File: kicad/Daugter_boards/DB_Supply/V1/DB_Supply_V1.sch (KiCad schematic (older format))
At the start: 30 parts, among them U1 LM555N

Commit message: update MDL and DB Supply
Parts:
- removed +12V1, +5V1: LM2940, symbol 78L05
- removed +3.3V: LM1117T, symbol 78L05
- removed -12V1, -5V1: LM2990, symbol 78L05
- added U2: LM2940T-12.0/NOPB, symbol LM2940T-12.0/NOPB
- added U3: LM2940T-5.0/NOPB, symbol LM2940T-5.0/NOPB
- added U4: LM1117T-3.3/NOPB, symbol LM1117T-3.3/NOPB
- added U5: LM2990T-12.0/NOPB, symbol LM2990T-12.0/NOPB
- added U6: LM2990T-5.0/NOPB, symbol LM2990T-5.0/NOPB
- D1: renamed from 1N400X1; value D -> 1N4001
- D2: renamed from 1N400X2; value D -> 1N4001
- D3: renamed from 1N400X3; value D -> 1N4001
- Q1: renamed from 2N2222; value Q_NPN_BCE -> Q2N2222
- Q2: renamed from 2N2222_1; value Q_NPN_BCE -> Q2N2222
- Q3: renamed from 2N2907; value Q_PNP_BCE -> Q2N2907
- gave numbers to parts that had none: 3
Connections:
- net at C9.1, P1.2 (P2), P2.2 (P2)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: now also U3.VO
- net at C1.1, C10.2, C2.1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: now also U2.GND, U3.GND, U4.GND, U5.GND, U6.GND
- net at C8.1, P1.6 (P6), P2.6 (P6): now also U2.VO, U3.VI, U4.VI
- net at C4.2, D3.2 (A): now also U5.VI
- net at C5.2, P1.8 (P8), P2.8 (P8): now also U5.VO, U6.VI
- net at C6.2, P1.18 (P18), P2.18 (P18): now also U6.VO
- net at C10.1, P1.19 (P19), P2.19 (P19): now also U4.VO
- net 18V: no longer names the net of C7.1, D1.1 (K), Q2.2 (C), R4.1
- net 18V: now also U2.VI
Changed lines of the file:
@@
 LIBS:contrib
 LIBS:valves
+LIBS:echopen
+LIBS:DB_Supply_V1-cache
 EELAYER 25 0
 EELAYER END
@@
 NoConn ~ 4750 3700
 $Comp
-L D 1N400X1
+L D D1
 U 1 1 572A15CB
 P 4900 5350
-F 0 "1N400X1" H 4900 5450 50  0000 C CNN
-F 1 "D" H 4900 5250 50  0000 C CNN
+F 0 "D1" H 4900 5450 50  0000 C CNN
+F 1 "1N4001" H 4900 5250 50  0000 C CNN
 F 2 "" H 4900 5350 50  0000 C CNN
 F 3 "" H 4900 5350 50  0000 C CNN
@@
 Connection ~ 6950 5800
 $Comp
-L Q_NPN_BCE 2N2222
+L Q_NPN_BCE Q1
 U 1 1 572A387C
 P 5600 3700
-F 0 "2N2222" H 5900 3750 50  0000 R CNN
-F 1 "Q_NPN_BCE" H 6200 3650 50  0000 R CNN
+F 0 "Q1" H 5900 3750 50  0000 R CNN
+F 1 "Q2N2222" H 6200 3650 50  0000 R CNN
 F 2 "" H 5800 3800 50  0000 C CNN
 F 3 "" H 5600 3700 50  0000 C CNN
@@
 	5050 3200 6600 3200
 $Comp
-L Q_NPN_BCE 2N2222_1
+L Q_NPN_BCE Q2
 U 1 1 572A3ACF
 P 6500 3400
-F 0 "2N2222_1" H 6800 3450 50  0000 R CNN
-F 1 "Q_NPN_BCE" H 7100 3350 50  0000 R CNN
+F 0 "Q2" H 6800 3450 50  0000 R CNN
+F 1 "Q2N2222" H 7100 3350 50  0000 R CNN
 F 2 "" H 6700 3500 50  0000 C CNN
 F 3 "" H 6500 3400 50  0000 C CNN
@@
 $EndComp
 $Comp
-L Q_PNP_BCE 2N2907
+L Q_PNP_BCE Q3
 U 1 1 572A3B5B
 P 6500 3800
-F 0 "2N2907" H 6800 3850 50  0000 R CNN
-F 1 "Q_PNP_BCE" H 7100 3750 50  0000 R CNN
+F 0 "Q3" H 6800 3850 50  0000 R CNN
+F 1 "Q2N2907" H 7100 3750 50  0000 R CNN
 F 2 "" H 6700 3900 50  0000 C CNN
 F 3 "" H 6500 3800 50  0000 C CNN
@@
 $EndComp
 $Comp
-L D 1N400X2
+L D D2
 U 1 1 572A3EDF
 P 7500 3750
-F 0 "1N400X2" H 7500 3850 50  0000 C CNN
-F 1 "D" H 7500 3650 50  0000 C CNN
+F 0 "D2" H 7500 3850 50  0000 C CNN
+F 1 "1N4001" H 7500 3650 50  0000 C CNN
 F 2 "" H 7500 3750 50  0000 C CNN
 F 3 "" H 7500 3750 50  0000 C CNN
@@
 $EndComp
 $Comp
-L D 1N400X3
+L D D3
 U 1 1 572A4183
 P 7650 3600
-F 0 "1N400X3" H 7650 3700 50  0000 C CNN
-F 1 "D" H 7650 3500 50  0000 C CNN
+F 0 "D3" H 7650 3700 50  0000 C CNN
+F 1 "1N4001" H 7650 3500 50  0000 C CNN
 F 2 "" H 7650 3600 50  0000 C CNN
 F 3 "" H 7650 3600 50  0000 C CNN
@@
 	5050 3200 5050 5500
 NoConn ~ 5050 3700
-$Comp
-L 78L05 -12V1
-U 1 1 575A0CF3
-P 8200 3650
-F 0 "-12V1" H 8350 3454 50  0000 C CNN
-F 1 "LM2990" H 8200 3850 50  0000 C CNN
-F 2 "" H 8200 3650 50  0000 C CNN
-F 3 "" H 8200 3650 50  0000 C CNN
-	1    8200 3650
-	1    0    0    -1
-$EndComp
-$Comp
-L 78L05 -5V1
-U 1 1 575A10F8
-P 9000 3650
-F 0 "-5V1" H 9150 3454 50  0000 C CNN
-F 1 "LM2990" H 9000 3850 50  0000 C CNN
-F 2 "" H 9000 3650 50  0000 C CNN
-F 3 "" H 9000 3650 50  0000 C CNN
-	1    9000 3650
-	1    0    0    -1
-$EndComp
 Connection ~ 8600 3600
 Wire Wire Line
@@
 	9400 4000 9400 3900
 Connection ~ 9000 4000
-$Comp
-L 78L05 +12V1
-U 1 1 575A672C
-P 5450 5400
-F 0 "+12V1" H 5600 5204 50  0000 C CNN
-F 1 "LM2940" H 5450 5600 50  0000 C CNN
-F 2 "" H 5450 5400 50  0000 C CNN
-F 3 "" H 5450 5400 50  0000 C CNN
-	1    5450 5400
-	1    0    0    -1
-$EndComp
-$Comp
-L 78L05 +5V1
-U 1 1 575A9393
-P 6250 5400
-F 0 "+5V1" H 6400 5204 50  0000 C CNN
-F 1 "LM2940" H 6250 5600 50  0000 C CNN
-F 2 "" H 6250 5400 50  0000 C CNN
-F 3 "" H 6250 5400 50  0000 C CNN
-	1    6250 5400
-	1    0    0    -1
-$EndComp
 Wire Wire Line
 	5850 4350 5850 5500
@@
 Connection ~ 7500 3600
 Connection ~ 5700 3500
-Text Label 6100 3200 0    60   ~ 0
-18V
 Text Label 8150 7650 0    60   ~ 0
 03/08/2016
@@
 Supply_daugter_board
 $Comp
-L CONN_01X19 P?
+L CONN_01X19 P1
 U 1 1 57A1CA2F
 P 2350 4850
-F 0 "P?" H 2350 5850 50  0000 C CNN
+F 0 "P1" H 2350 5850 50  0000 C CNN
 F 1 "CONN_01X19" V 2450 4850 50  0000 C CNN
 F 2 "" H 2350 4850 50  0000 C CNN
@@
 Wire Wire Line
 	8600 2850 8600 3600
-$Comp
-L 78L05 +3.3V
-U 1 1 57A2E6B8
-P 6300 4400
-F 0 "+3.3V" H 6450 4204 50  0000 C CNN
-F 1 "LM1117T" H 6300 4600 50  0000 C CNN
-F 2 "" H 6300 4400 50  0000 C CNN
-F 3 "" H 6300 4400 50  0000 C CNN
-	1    6300 4400
-	1    0    0    -1
-$EndComp
 Wire Wire Line
 	5850 4350 5900 4350
 Connection ~ 5850 5050
 $Comp
-L CP C?
+L CP C10
 U 1 1 57A2E7D0
 P 6700 4500
-F 0 "C?" H 6725 4600 50  0000 L CNN
+F 0 "C10" H 6725 4600 50  0000 L CNN
 F 1 "47u" H 6725 4400 50  0000 L CNN
 F 2 "" H 6738 4350 50  0000 C CNN
@@
 NoConn ~ 5850 4850
 $Comp
-L CONN_01X19 P?
+L CONN_01X19 P2
 U 1 1 57A31EE2
 P 10650 4850
-F 0 "P?" H 10650 5850 50  0000 C CNN
+F 0 "P2" H 10650 5850 50  0000 C CNN
 F 1 "CONN_01X19" V 10750 4850 50  0000 C CNN
 F 2 "" H 10650 4850 50  0000 C CNN
@@
 NoConn ~ 9900 3950
 NoConn ~ 9900 4050
+$Comp
+L LM2940T-12.0/NOPB U2
+U 1 1 57AB2B24
+P 5450 5400
+F 0 "U2" H 5600 5204 50  0000 C CNN
+F 1 "LM2940T-12.0/NOPB" H 5450 5600 50  0000 C CNN
+F 2 "" H 5450 5400 50  0000 C CNN
+F 3 "" H 5450 5400 50  0000 C CNN
+	1    5450 5400
+	1    0    0    -1
+$EndComp
+$Comp
+L LM2940T-5.0/NOPB U3
+U 1 1 57AB2BC1
+P 6250 5400
+F 0 "U3" H 6400 5204 50  0000 C CNN
+F 1 "LM2940T-5.0/NOPB" H 6250 5600 50  0000 C CNN
+F 2 "" H 6250 5400 50  0000 C CNN
+F 3 "" H 6250 5400 50  0000 C CNN
+	1    6250 5400
+	1    0    0    -1
+$EndComp
+$Comp
+L LM1117T-3.3/NOPB U4
+U 1 1 57AB2C54
+P 6300 4400
+F 0 "U4" H 6450 4204 50  0000 C CNN
+F 1 "LM1117T-3.3/NOPB" H 6300 4600 50  0000 C CNN
+F 2 "" H 6300 4400 50  0000 C CNN
+F 3 "" H 6300 4400 50  0000 C CNN
+	1    6300 4400
+	1    0    0    -1
+$EndComp
+$Comp
+L LM2990T-12.0/NOPB U5
+U 1 1 57AB4084
+P 8200 3650
+F 0 "U5" H 8350 3454 50  0000 C CNN
+F 1 "LM2990T-12.0/NOPB" H 8200 3850 50  0000 C CNN
+F 2 "" H 8200 3650 50  0000 C CNN
+F 3 "" H 8200 3650 50  0000 C CNN
+	1    8200 3650
+	1    0    0    -1
+$EndComp
+$Comp
+L LM2990T-5.0/NOPB U6
+U 1 1 57AB4135
+P 9000 3650
+F 0 "U6" H 9150 3454 50  0000 C CNN
+F 1 "LM2990T-5.0/NOPB" H 9000 3850 50  0000 C CNN
+F 2 "" H 9000 3650 50  0000 C CNN
+F 3 "" H 9000 3650 50  0000 C CNN
+	1    9000 3650
+	1    0    0    -1
+$EndComp
 $EndSCHEMATC

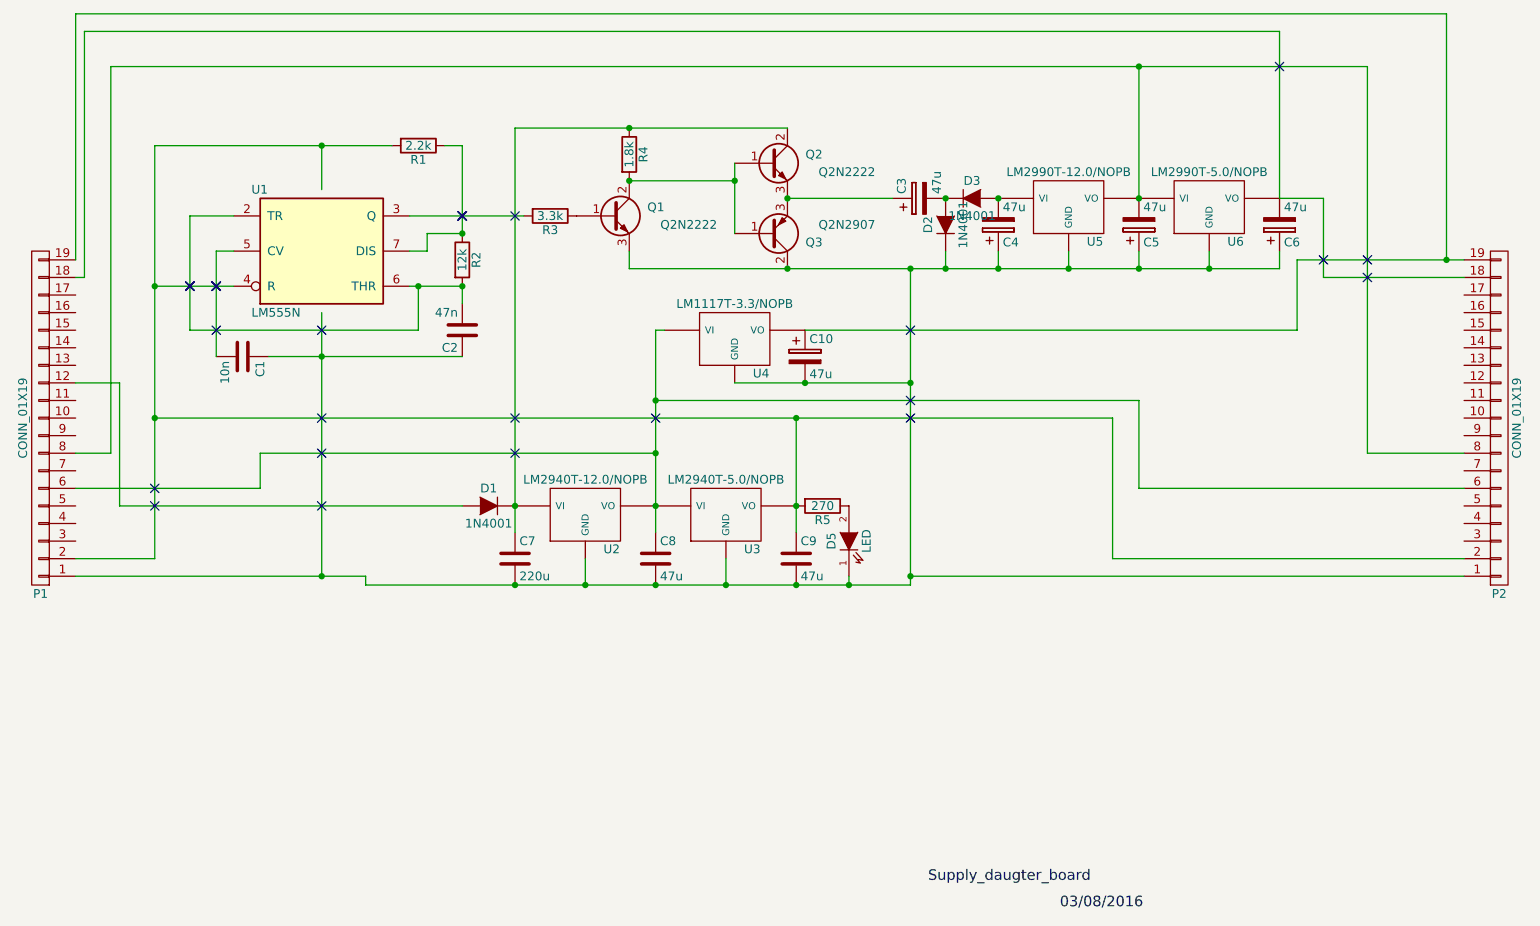
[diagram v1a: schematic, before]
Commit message: update DB_HV, update librairy and librairy path for MDL
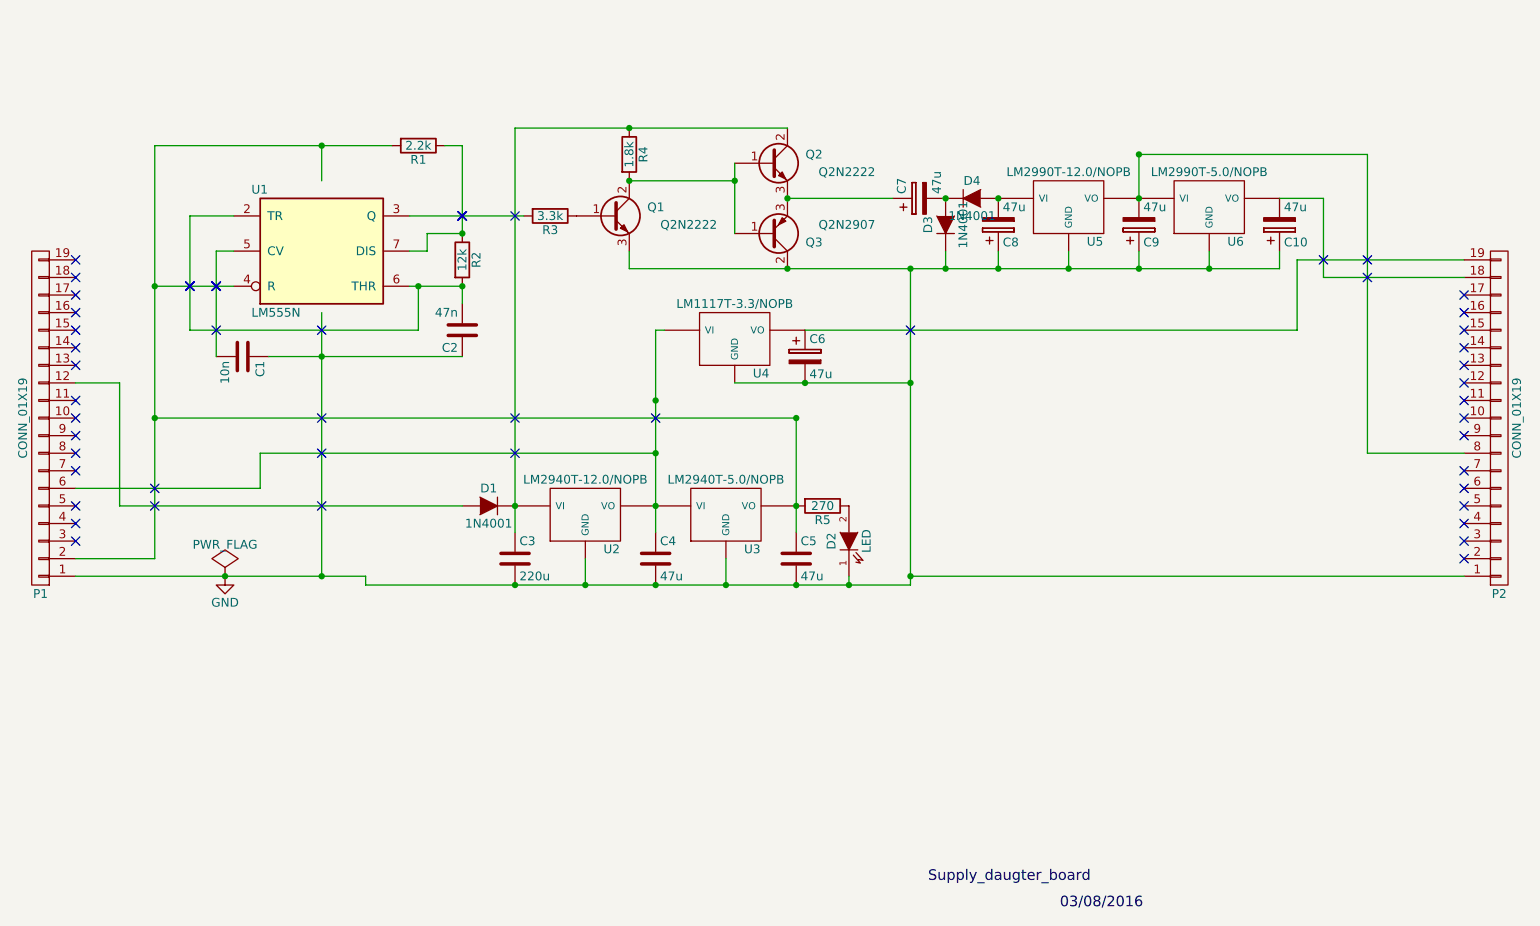
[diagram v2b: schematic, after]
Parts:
- C1, C2: footprint (none) -> Capacitors_ThroughHole:C_Disc_D6_P5
- C10: renamed from C6; footprint (none) -> Capacitors_ThroughHole:C_Radial_D5_L6_P2.5
- C3: renamed from C7; footprint (none) -> Capacitors_ThroughHole:C_Radial_D8_L11.5_P3.5
- C4: renamed from C8; footprint (none) -> Capacitors_ThroughHole:C_Radial_D5_L6_P2.5
- C5: renamed from C9; footprint (none) -> Capacitors_ThroughHole:C_Radial_D5_L6_P2.5
- C6: renamed from C10; footprint (none) -> Capacitors_ThroughHole:C_Radial_D5_L6_P2.5
- C7: renamed from C3; footprint (none) -> Capacitors_ThroughHole:C_Radial_D5_L6_P2.5
- C8: renamed from C4; footprint (none) -> Capacitors_ThroughHole:C_Radial_D5_L6_P2.5
- C9: renamed from C5; footprint (none) -> Capacitors_ThroughHole:C_Radial_D5_L6_P2.5
- D1: footprint (none) -> Diodes_ThroughHole:Diode_DO-35_SOD27_Horizontal_RM10
- D2: renamed from D5; footprint (none) -> LEDs:LED-5MM
- D3: renamed from D2; footprint (none) -> Diodes_ThroughHole:Diode_DO-35_SOD27_Horizontal_RM10
- D4: renamed from D3; footprint (none) -> Diodes_ThroughHole:Diode_DO-35_SOD27_Horizontal_RM10
- P1, P2: footprint (none) -> Socket_Strips:Socket_Strip_Straight_1x19
- Q1, Q2, Q3: footprint (none) -> TO_SOT_Packages_THT:TO-18_3Pin
- R1, R2, R3, R4, R5: footprint (none) -> Resistors_ThroughHole:Resistor_Horizontal_RM7mm
- U1: footprint (none) -> Power_Integrations:PDIP-8
- U2, U3, U4, U5, U6: footprint (none) -> TO_SOT_Packages_THT:TO-220_Neutral123_Vertical
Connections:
- net GND: now also C1.1, C10.1, C2.1, C3.2, C4.2, C5.2, C6.2, C8.1, C9.1, D2.1 (K), D3.1 (K), P1.1 (P1), P2.1 (P1), Q1.3 (E), Q3.2 (C), U2.GND, U3.GND, U4.GND, U5.GND, U6.GND
- net VCC: now also C5.1, P1.2 (P2), R1.2, R5.2, U1.4 (R), U3.VO
- net at C4.1, P1.6 (P6), U2.VO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: no longer P2.6 (P6)
- net at C9.2, P2.8 (P8), U5.VO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: no longer P1.8 (P8)
- net at C10.2, P2.18 (P18), U6.VO: no longer P1.18 (P18)
- net at C6.1, P2.19 (P19), U4.VO: no longer P1.19 (P19)
- now unconnected: P2.2 (P2)
- no-connect marks 30 -> 57
